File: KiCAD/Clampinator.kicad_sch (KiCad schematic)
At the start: 119 parts, among them J2 Conn_01x02_Socket, J20 VP0365840000G, J21 Conn_01x03_Socket, J22 Conn_01x03_Socket, J23 VP0265840000G, J24 VP0365840000G, J25 +5V INJ, J3 Conn_01x02_Socket, J4 Conn_01x02_Socket, Q1 TK100E10N1,S1X, Q2 TK100E10N1,S1X, Q3 TK100E10N1,S1X, Q4 TK100E10N1,S1X, Q5 TK100E10N1,S1X, Q6 TK100E10N1,S1X, Q9 MMBT3904-C20526, SW6 EG1847-ND, SW7 GPI-154-3013, U10 LM74810QDRRRQ1, U14 LM5163DDAR, U2 TL432BQDBZR, U3 EG2131, U4 UCC33420RAQR_C46461551, U6 LM5012DDAR, U9 EL357N

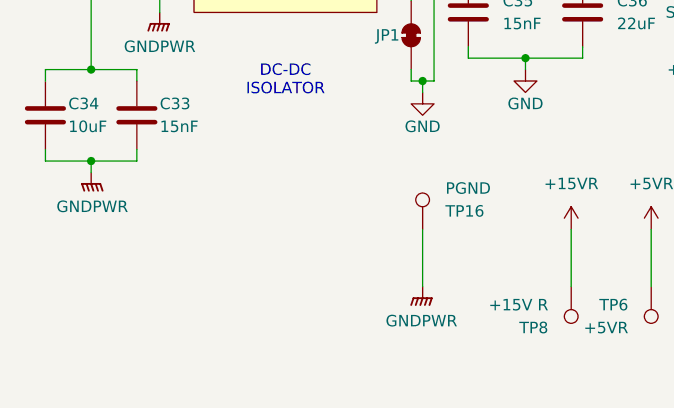
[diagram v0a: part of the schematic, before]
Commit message: Extra PGND test pads for ground noise/bounce testing
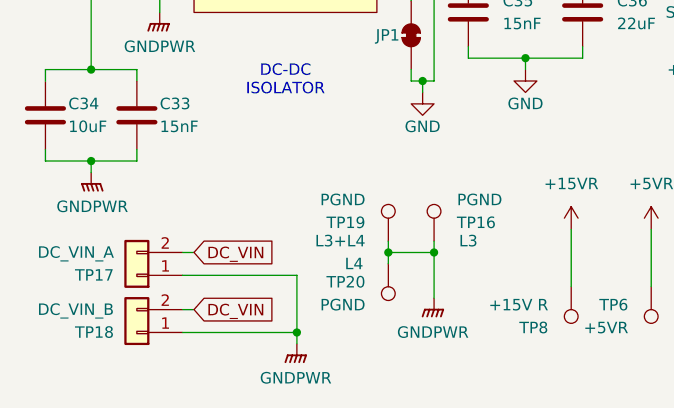
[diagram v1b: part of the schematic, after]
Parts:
- added TP17: DC_VIN_A, Connector_PinHeader_2.54mm:PinHeader_1x02_P2.54mm_Vertical, symbol Connector_Generic:Conn_01x02
- added TP18: DC_VIN_B, Connector_PinHeader_2.54mm:PinHeader_1x02_P2.54mm_Vertical, symbol Connector_Generic:Conn_01x02
- added TP19, TP20: PGND, TestPoint:TestPoint_THTPad_D2.0mm_Drill1.0mm, symbol Connector:TestPoint
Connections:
- net DC_VIN: now also TP17.2 (Pin_2), TP18.2 (Pin_2)
- net GNDPWR: now also TP17.1 (Pin_1), TP18.1 (Pin_1), TP19.1, TP20.1
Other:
- moved on the sheet: TP16
